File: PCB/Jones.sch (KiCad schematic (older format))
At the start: 220 parts, among them J1 USB4085-GF-A_REVA, U2 ATmega32U4-MU, Y1 16MHz

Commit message: VIAで5レイヤー使えるようにするため、総当たりマトリクスを10ピンから9ピンへ変更
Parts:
- removed LED3, LED4: SK6812MINI, LED_SMD:LED_SK6812MINI_PLCC4_3.5x3.5mm_P1.75mm_TriangleMark, symbol LED:SK6812MINI
- added D89: D, SMK_ai03_RandomKeyboardParts:D_SOD-123-Pretty, symbol Device:D
- added SW_LSFT1u1, SW_LSFT1u2: SW_Push, MX_Alps_Hybrid:MXOnly-1U-Hotswap, symbol Switch:SW_Push
- renumbered D86 to D0, D84 to D1, D71 to D10, D61 to D12, D51 to D13, D37 to D14, D33 to D15, D25 to D16, D16 to D17, D11 to D18, D1 to D19, D85 to D2, D57 to D21, D52 to D23, D47 to D24, D42 to D25, D17 to D27, D12 to D28, D2 to D29, D83 to D3, D58 to D31, D53 to D32, D48 to D34, D43 to D35, D27 to D36, D18 to D37, D13 to D38, D3 to D39, D81 to D4, D59 to D41, D36 to D42, D44 to D43, D40 to D45, D24 to D46, D14 to D47, D9 to D48, D4 to D49, D79 to D5, D65 to D51, D60 to D52, D45 to D53, D69 to D54, D20 to D56, D15 to D57, D10 to D58, D5 to D59, D77 to D6, D62 to D61, D56 to D62, D46 to D63, D41 to D64, D29 to D65, D21 to D67, D6 to D68, D7 to D69, D75 to D7, D63 to D71, D54 to D72, D34 to D73, D30 to D74, D38 to D75, D22 to D78, D8 to D79, D73 to D8, D64 to D81, D55 to D82, D35 to D83, D31 to D84, D39 to D85, D23 to D87, D66 to D9, D70 to D91, D50 to D92, D32 to D93, D49 to D94, D28 to D95, D68 to D96, D19 to D97, D67 to D98, LED5 to LED3, LED6 to LED4, LED7 to LED5, LED8 to LED6
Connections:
- net labels removed: pin10
- wire segments 405 -> 421
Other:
- moved on the sheet: D2, D23, D24, D25, D26, D27, D28, D3, D32, D34, D35, D36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

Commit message: ロングスペース左Mod変更
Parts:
- removed SW_CAPS1.25u1: SW_Push, MX_Alps_Hybrid:MXOnly-1.25U-NoLED, symbol Switch:SW_Push
- SW_LongOPT1.25: renamed from SW_LongOPT1; footprint MX_Alps_Hybrid:MXOnly-1U-Hotswap -> MX_Alps_Hybrid:MXOnly-1.25U-Hotswap
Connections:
- wire segments 421 -> 419
- no-connect marks 11 -> 12
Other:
- moved on the sheet: SW_CAPS1u1
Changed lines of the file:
@@
 	0    -1   -1   0
 $EndComp
+NoConn ~ 15275 2650
 $Comp
-L Switch:SW_Push SW_LongOPT1
+L Switch:SW_Push SW_CAPS1u1
+U 1 1 5F67807F
+P 1125 7075
+F 0 "SW_CAPS1u1" H 1125 7360 50  0000 C CNN
+F 1 "SW_Push" H 1125 7269 50  0000 C CNN
+F 2 "MX_Alps_Hybrid:MXOnly-1U-Hotswap" H 1125 7275 50  0001 C CNN
+F 3 "~" H 1125 7275 50  0001 C CNN
+	1    1125 7075
+	1    0    0    -1
+$EndComp
+Connection ~ 1325 7075
+Wire Wire Line
+	1325 6825 1325 7075
+Wire Wire Line
+	925  5825 925  7075
+$Comp
+L Switch:SW_Push SW_LongOPT1.25
 U 1 1 5F29DC6B
 P 1775 7075
-F 0 "SW_LongOPT1" H 1775 7360 50  0000 C CNN
+F 0 "SW_LongOPT1.25" H 1775 7360 50  0000 C CNN
 F 1 "SW_Push" H 1775 7269 50  0000 C CNN
-F 2 "MX_Alps_Hybrid:MXOnly-1U-Hotswap" H 1775 7275 50  0001 C CNN
+F 2 "MX_Alps_Hybrid:MXOnly-1.25U-Hotswap" H 1775 7275 50  0001 C CNN
 F 3 "~" H 1775 7275 50  0001 C CNN
 	1    1775 7075
 	1    0    0    -1
 $EndComp
-Wire Wire Line
-	925  5825 925  6925
-Wire Wire Line
-	925  6925 925  7075
-Connection ~ 925  6925
-Wire Wire Line
-	1325 7075 1325 6925
-Wire Wire Line
-	1325 6925 1325 6825
-Connection ~ 1325 6925
-$Comp
-L Switch:SW_Push SW_CAPS1u1
-U 1 1 5F67807F
-P 1125 6925
-F 0 "SW_CAPS1u1" H 1125 7210 50  0000 C CNN
-F 1 "SW_Push" H 1125 7119 50  0000 C CNN
-F 2 "MX_Alps_Hybrid:MXOnly-1U-Hotswap" H 1125 7125 50  0001 C CNN
-F 3 "~" H 1125 7125 50  0001 C CNN
-	1    1125 6925
-	1    0    0    -1
-$EndComp
-Connection ~ 1325 7075
-$Comp
-L Switch:SW_Push SW_CAPS1.25u1
-U 1 1 5F02207D
-P 1125 7075
-F 0 "SW_CAPS1.25u1" H 1125 7360 50  0000 C CNN
-F 1 "SW_Push" H 1125 7269 50  0000 C CNN
-F 2 "MX_Alps_Hybrid:MXOnly-1.25U-NoLED" H 1125 7275 50  0001 C CNN
-F 3 "~" H 1125 7275 50  0001 C CNN
-	1    1125 7075
-	1    0    0    -1
-$EndComp

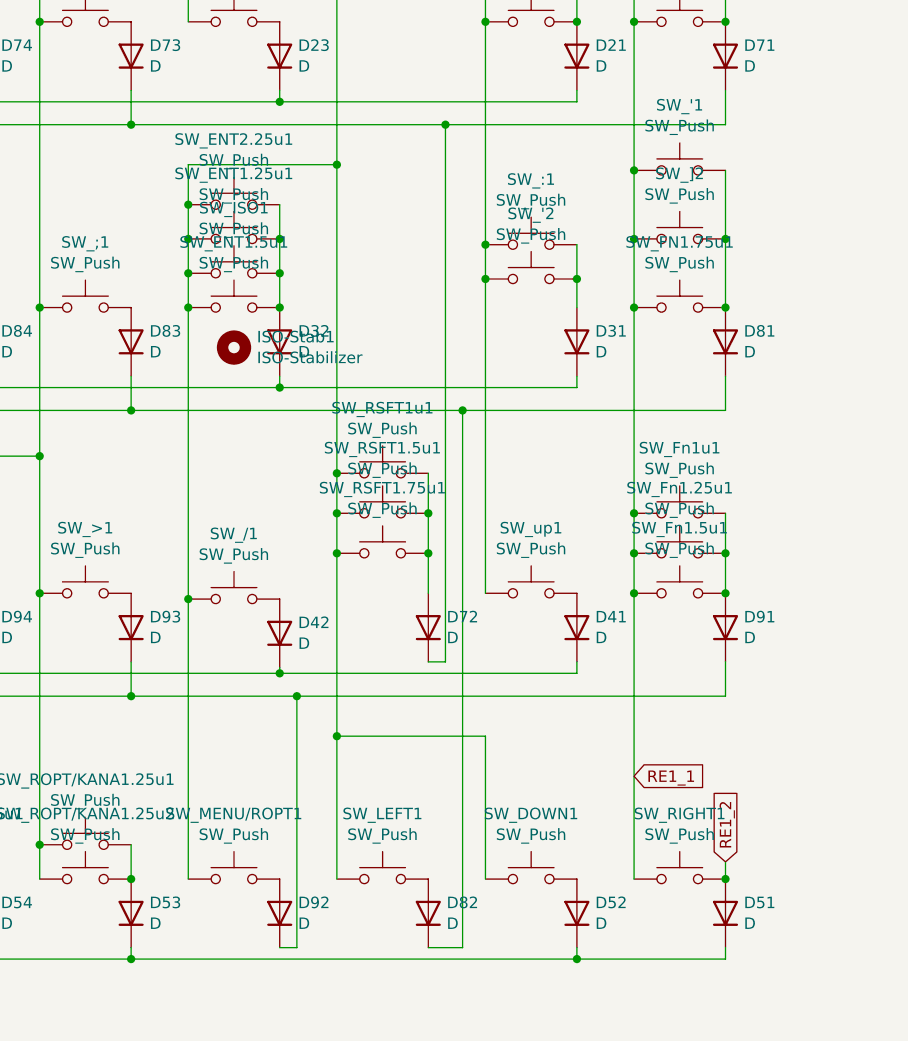
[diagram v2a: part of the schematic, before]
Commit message: Enter 1.25uとその右の関連を削除。右Shift 1.5+1.5を削除。
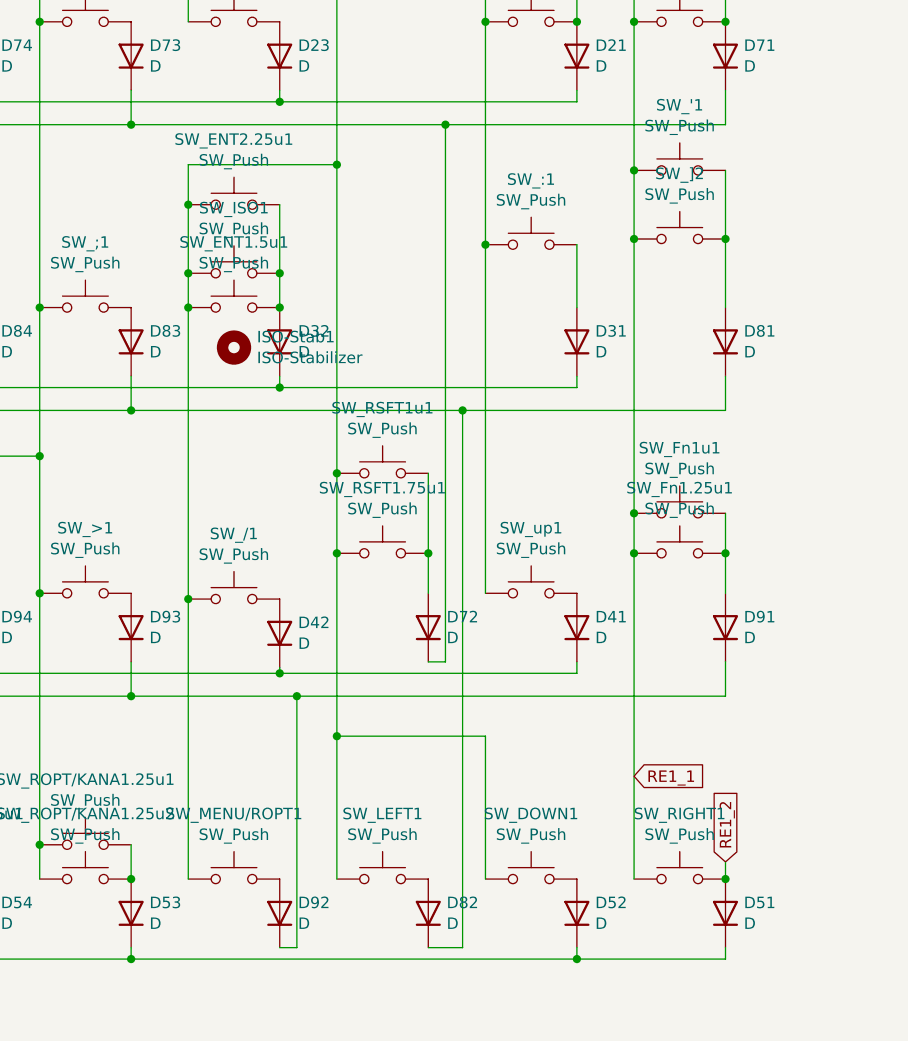
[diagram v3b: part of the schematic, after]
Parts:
- removed SW_'2: SW_Push, MX_Alps_Hybrid:MXOnly-1U-NoLED, symbol Switch:SW_Push
- removed SW_ENT1.25u1: SW_Push, MX_Alps_Hybrid:MXOnly-1.25U-NoLED, symbol Switch:SW_Push
- removed SW_FN1.75u1: SW_Push, MX_Alps_Hybrid:MXOnly-1.75U-NoLED, symbol Switch:SW_Push
- removed SW_Fn1.5u1, SW_RSFT1.5u1: SW_Push, MX_Alps_Hybrid:MXOnly-1.5U-NoLED, symbol Switch:SW_Push
- SW_ENT1.5u1: footprint MX_Alps_Hybrid:MXOnly-1.5U-NoLED -> MX_Alps_Hybrid:MXOnly-1.5U-Hotswap
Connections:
- wire segments 419 -> 411
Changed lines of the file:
@@
-$EndComp
-$Comp
-L Switch:SW_Push SW_RSFT1.5u1
-U 1 1 5F66BA37
-P 8925 5475
-F 0 "SW_RSFT1.5u1" H 8925 5760 50  0000 C CNN
-F 1 "SW_Push" H 8925 5669 50  0000 C CNN
-F 2 "MX_Alps_Hybrid:MXOnly-1.5U-NoLED" H 8925 5675 50  0001 C CNN
-F 3 "~" H 8925 5675 50  0001 C CNN
-	1    8925 5475
-	1    0    0    -1
 $EndComp
 $Comp
@@
 F 3 "~" H 2425 7275 50  0001 C CNN
 	1    2425 7075
-	1    0    0    -1
-$EndComp
-$Comp
-L Switch:SW_Push SW_'2
-U 1 1 5F68651C
-P 9575 4450
-F 0 "SW_'2" H 9575 4735 50  0000 C CNN
-F 1 "SW_Push" H 9575 4644 50  0000 C CNN
-F 2 "MX_Alps_Hybrid:MXOnly-1U-NoLED" H 9575 4650 50  0001 C CNN
-F 3 "~" H 9575 4650 50  0001 C CNN
-	1    9575 4450
 	1    0    0    -1
 $EndComp
@@
 	1    0    0    -1
 $EndComp
-Wire Wire Line
-	9125 5300 9125 5475
 $Comp
 L power:PWR_FLAG #FLG01
@@
 	0    -1   -1   0
 $EndComp
-Wire Wire Line
-	9775 4450 9775 4575
 $Comp
 L Device:D D31
@@
 F 0 "SW_ENT1.5u1" H 8275 4860 50  0000 C CNN
 F 1 "SW_Push" H 8275 4769 50  0000 C CNN
-F 2 "MX_Alps_Hybrid:MXOnly-1.5U-NoLED" H 8275 4775 50  0001 C CNN
+F 2 "MX_Alps_Hybrid:MXOnly-1.5U-Hotswap" H 8275 4775 50  0001 C CNN
 F 3 "~" H 8275 4775 50  0001 C CNN
 	1    8275 4575
@@
 	8075 4425 8075 4575
 Connection ~ 8475 4575
-Connection ~ 9375 4450
-$Comp
-L Switch:SW_Push SW_FN1.75u1
-U 1 1 61BAA342
-P 10225 4575
-F 0 "SW_FN1.75u1" H 10225 4860 50  0000 C CNN
-F 1 "SW_Push" H 10225 4769 50  0000 C CNN
-F 2 "MX_Alps_Hybrid:MXOnly-1.75U-NoLED" H 10225 4775 50  0001 C CNN
-F 3 "~" H 10225 4775 50  0001 C CNN
-	1    10225 4575
-	1    0    0    -1
-$EndComp
 Connection ~ 10025 3975
 Connection ~ 10025 4275
-Connection ~ 10025 4575
-Wire Wire Line
-	10025 4575 10025 5475
-Connection ~ 10425 4575
-Connection ~ 10425 5825
-$Comp
-L Switch:SW_Push SW_Fn1.5u1
-U 1 1 5F3CB957
-P 10225 5825
-F 0 "SW_Fn1.5u1" H 10225 6110 50  0000 C CNN
-F 1 "SW_Push" H 10225 6019 50  0000 C CNN
-F 2 "MX_Alps_Hybrid:MXOnly-1.5U-NoLED" H 10225 6025 50  0001 C CNN
-F 3 "~" H 10225 6025 50  0001 C CNN
-	1    10225 5825
-	1    0    0    -1
-$EndComp
 $Comp
 L Switch:SW_Push SW_RSFT1.75u1
@@
 Wire Wire Line
 	9125 5650 9125 5825
-Connection ~ 8725 5475
-Wire Wire Line
-	8725 5475 8725 5650
 $Comp
 L Switch:SW_Push SW_RSFT1u1
@@
 	1    0    0    -1
 $EndComp
-Connection ~ 9125 5475
-Wire Wire Line
-	9125 5475 9125 5650
-Wire Wire Line
-	8725 5300 8725 5475
 Connection ~ 10025 5475
 Wire Wire Line
 	10025 5475 10025 5650
 Connection ~ 10025 5650
-Wire Wire Line
-	10025 5650 10025 5825
-Connection ~ 10025 5825
-Wire Wire Line
-	10025 5825 10025 7075
 Text GLabel 10025 1175 1    50   Input ~ 0
 pin1
@@
 $EndComp
 Wire Wire Line
-	8075 4125 8075 4275
-Wire Wire Line
-	8475 4125 8475 4275
-Wire Wire Line
-	9375 4450 9375 5825
-Wire Wire Line
 	10025 3975 10025 4275
 Wire Wire Line
@@
 	5325 9250 5525 9250
 $Comp
-L Switch:SW_Push SW_ENT1.25u1
-U 1 1 5FDEE168
-P 8275 4275
-F 0 "SW_ENT1.25u1" H 8275 4560 50  0000 C CNN
-F 1 "SW_Push" H 8275 4469 50  0000 C CNN
-F 2 "MX_Alps_Hybrid:MXOnly-1.25U-NoLED" H 8275 4475 50  0001 C CNN
-F 3 "~" H 8275 4475 50  0001 C CNN
-	1    8275 4275
-	1    0    0    -1
-$EndComp
-Connection ~ 8075 4275
-Wire Wire Line
-	8075 4275 8075 4425
-Connection ~ 8475 4275
-Wire Wire Line
-	8475 4275 8475 4425
-$Comp
 L Switch:SW_Push SW_:1
 U 1 1 5FE08221
@@
 $EndComp
 Wire Wire Line
-	9775 4300 9775 4450
-Connection ~ 9775 4450
-Wire Wire Line
-	10025 4275 10025 4575
-Wire Wire Line
 	10425 4275 10425 4575
 Text GLabel 10425 7000 1    50   Input ~ 0
@@
 RE1_1
 Connection ~ 9375 4300
-Wire Wire Line
-	9375 4300 9375 4450
 $Comp
 L Switch:SW_Push SW_ESC2
@@
 	1    0    0    -1
 $EndComp
+Wire Wire Line
+	8075 4125 8075 4425
+Wire Wire Line
+	8475 4125 8475 4425
+Wire Wire Line
+	9375 4300 9375 5825
+Wire Wire Line
+	9775 4300 9775 4575
+Wire Wire Line
+	10025 4275 10025 5475
+Wire Wire Line
+	8725 5300 8725 5650
+Wire Wire Line
+	9125 5300 9125 5650
+Wire Wire Line
+	10025 5650 10025 7075
 $EndSCHEMATC

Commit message: 穴の干渉を減らすため、ISOエンターのスタビの方向を逆に。
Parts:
- ISO-Stab1: footprint MX_Alps_Hybrid:MXOnly-ISO-StabilizerOnly-Reversed -> MX_Alps_Hybrid:MXOnly-ISO-StabilizerOnly
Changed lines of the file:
@@
 F 0 "ISO-Stab1" H 8375 4796 50  0000 L CNN
 F 1 "ISO-Stabilizer" H 8375 4705 50  0000 L CNN
-F 2 "MX_Alps_Hybrid:MXOnly-ISO-StabilizerOnly-Reversed" H 8275 4750 50  0001 C CNN
+F 2 "MX_Alps_Hybrid:MXOnly-ISO-StabilizerOnly" H 8275 4750 50  0001 C CNN
 F 3 "~" H 8275 4750 50  0001 C CNN
 	1    8275 4750

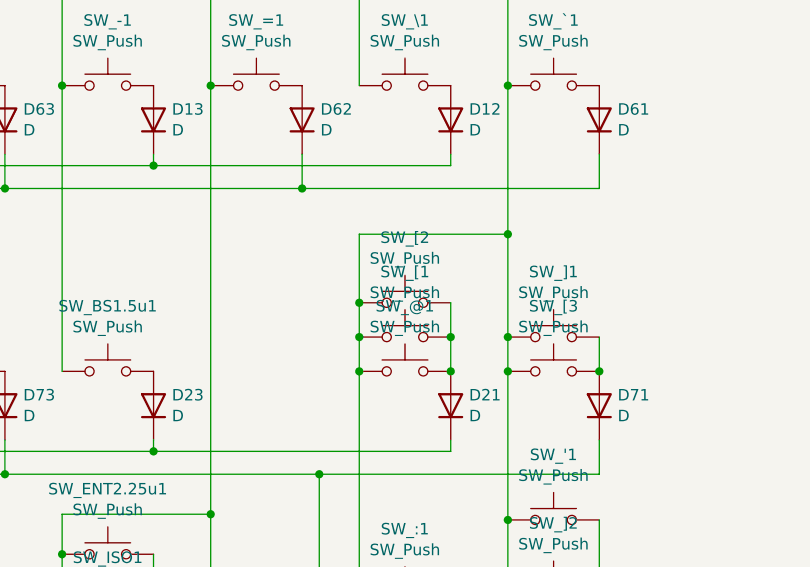
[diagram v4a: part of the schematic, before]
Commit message: 右上ネジ穴にかぶるソケットのプラ部分の干渉対策。
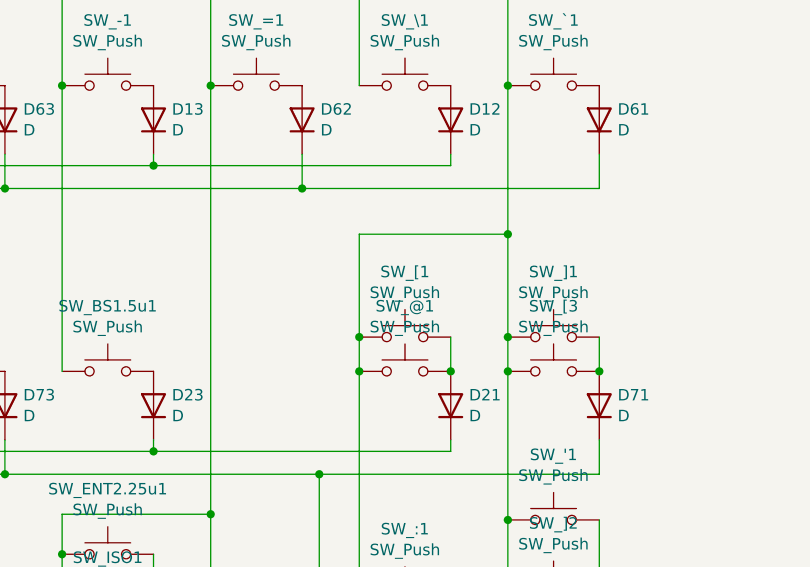
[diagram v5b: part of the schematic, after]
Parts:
- removed SW_[2: SW_Push, MX_Alps_Hybrid:MXOnly-1U-NoLED, symbol Switch:SW_Push
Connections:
- wire segments 411 -> 409
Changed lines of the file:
@@
 Connection ~ 9775 3325
-$Comp
-L Switch:SW_Push SW_[2
-U 1 1 5FB0372F
-P 9575 3025
-F 0 "SW_[2" H 9575 3310 50  0000 C CNN
-F 1 "SW_Push" H 9575 3219 50  0000 C CNN
-F 2 "MX_Alps_Hybrid:MXOnly-1U-NoLED" H 9575 3225 50  0001 C CNN
-F 3 "~" H 9575 3225 50  0001 C CNN
-	1    9575 3025
-	1    0    0    -1
-$EndComp
-Wire Wire Line
-	9775 3025 9775 3175
-Connection ~ 9775 3175
-Wire Wire Line
-	9375 3025 9375 3175
 $Comp
 L Jumper:SolderJumper_3_Open JP_LED2
@@
 Wire Wire Line
 	10025 2725 9375 2725
-Wire Wire Line
-	9375 2725 9375 3025
 Connection ~ 10025 2725
 Wire Wire Line
 	10025 2725 10025 3175
-Connection ~ 9375 3025
 Wire Wire Line
 	8725 6450 9375 6450
@@
 Wire Wire Line
 	10025 5650 10025 7075
+Wire Wire Line
+	9375 2725 9375 3175
 $EndSCHEMATC

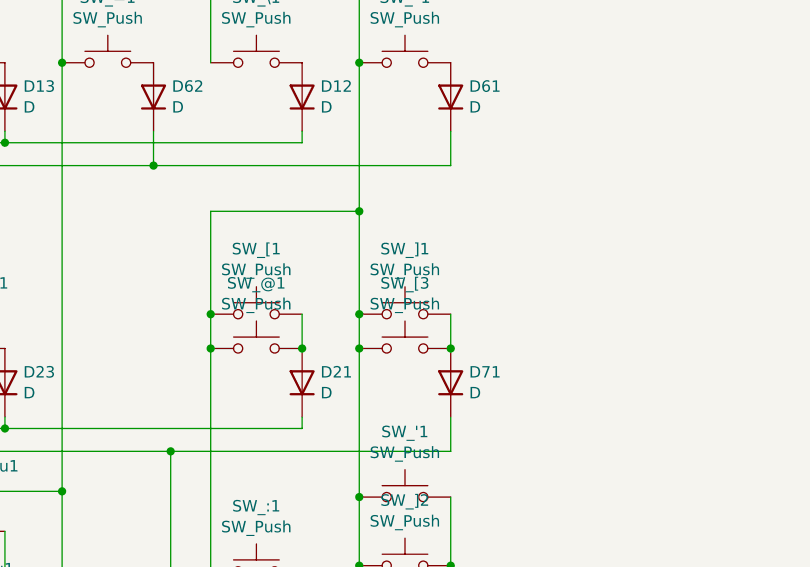
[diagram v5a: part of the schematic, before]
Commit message: 右上ネジ穴にかぶるソケットのプラ部分の干渉対策。
右隣のフットプリントとパッドの干渉があったため、さらに修正。
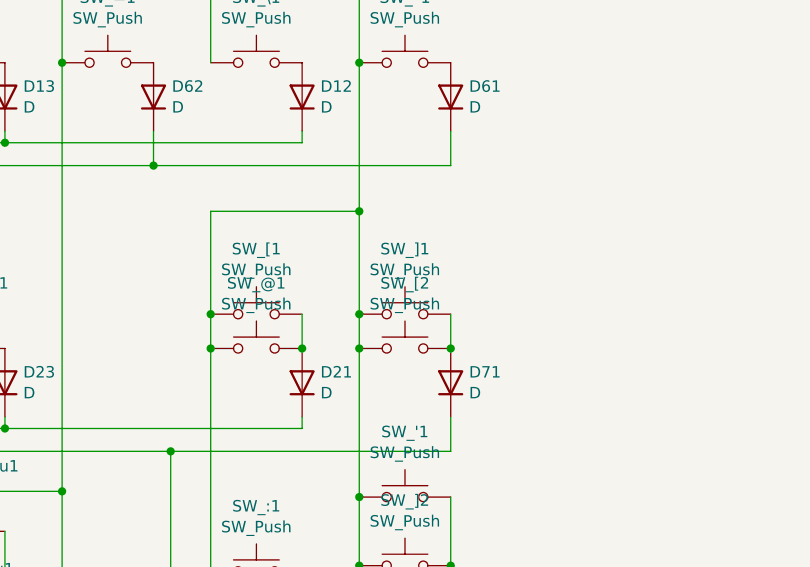
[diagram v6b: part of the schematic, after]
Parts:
- renumbered SW_[3 to SW_[2
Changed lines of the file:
@@
 	10025 2075 10025 2725
 $Comp
-L Switch:SW_Push SW_[3
+L Switch:SW_Push SW_[2
 U 1 1 61629E68
 P 10225 3325
-F 0 "SW_[3" H 10225 3610 50  0000 C CNN
+F 0 "SW_[2" H 10225 3610 50  0000 C CNN
 F 1 "SW_Push" H 10225 3519 50  0000 C CNN
 F 2 "MX_Alps_Hybrid:MXOnly-1U-Hotswap" H 10225 3525 50  0001 C CNN

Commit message: 1uソケットのフットプリントにガイド線追加
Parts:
- SW_'1, SW_-1, SW_/1, SW_0, SW_1_1, SW_2, SW_3, SW_4, SW_5, SW_6, SW_7, SW_8, SW_9, SW_:1, SW_;1, SW_<1, SW_=1, SW_>1, SW_@1, SW_A1, SW_B1, SW_C1, SW_D1, SW_DOWN1, SW_E1, SW_ESC1, SW_F1, SW_Fn1u1, SW_G1, SW_H1, SW_I1, SW_ISO1, SW_J1, SW_K1, SW_L1, SW_LEFT1, SW_LSFT1u1, SW_LSFT1u2, SW_M1, SW_N1, SW_O1, SW_P1, SW_Q1, SW_R1, SW_RIGHT1, SW_RSFT1u1, SW_S1, SW_T1, SW_U1, SW_V1, SW_W1, SW_WIN1, SW_X1, SW_Y1, SW_Z1, SW_[1, SW_[2, SW_\1, SW_]1, SW_]2, SW_`1, SW_up1: footprint MX_Alps_Hybrid:MXOnly-1U-Hotswap -> MX_Alps_Hybrid:MXOnly-1U-Hotswap-guide
